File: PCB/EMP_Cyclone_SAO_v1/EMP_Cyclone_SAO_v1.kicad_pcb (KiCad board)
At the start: 2 copper layers, 72.8 x 84.4 mm, 7 parts, among them SW1 SW_Push, SW2 SW_Push, U3 ESP32-C3_SUPERMINI

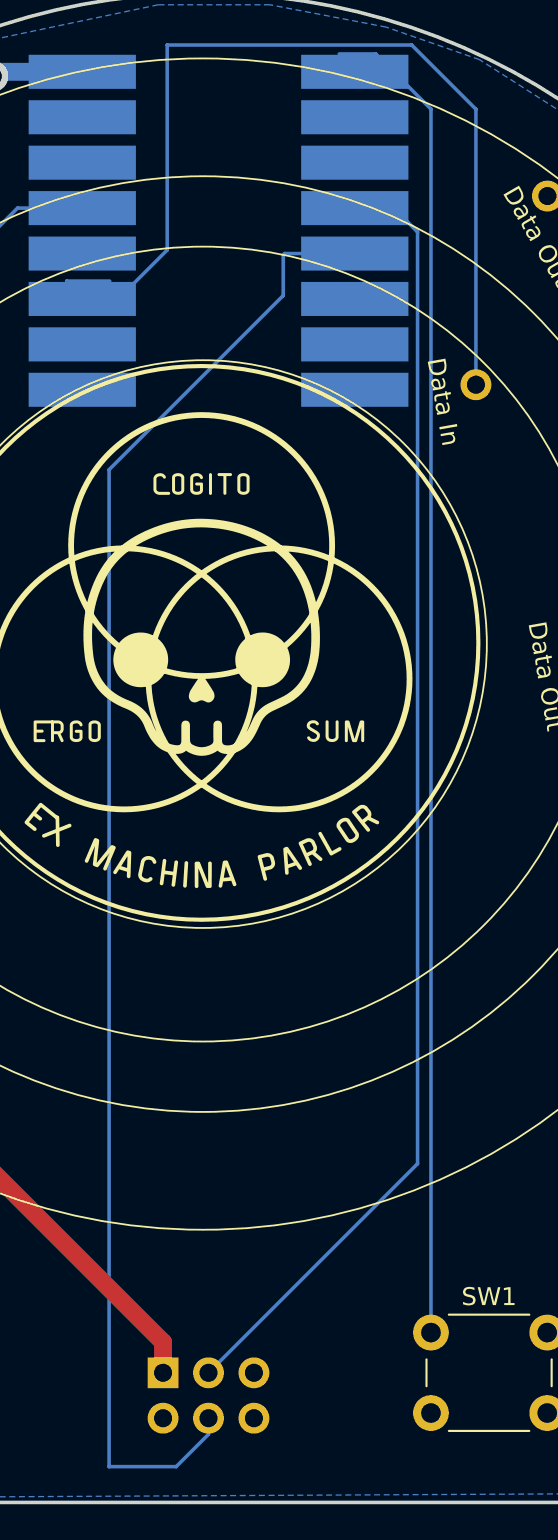
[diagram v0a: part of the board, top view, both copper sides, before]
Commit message: EMP SAO v2.1. Gerber files updated and ordered.
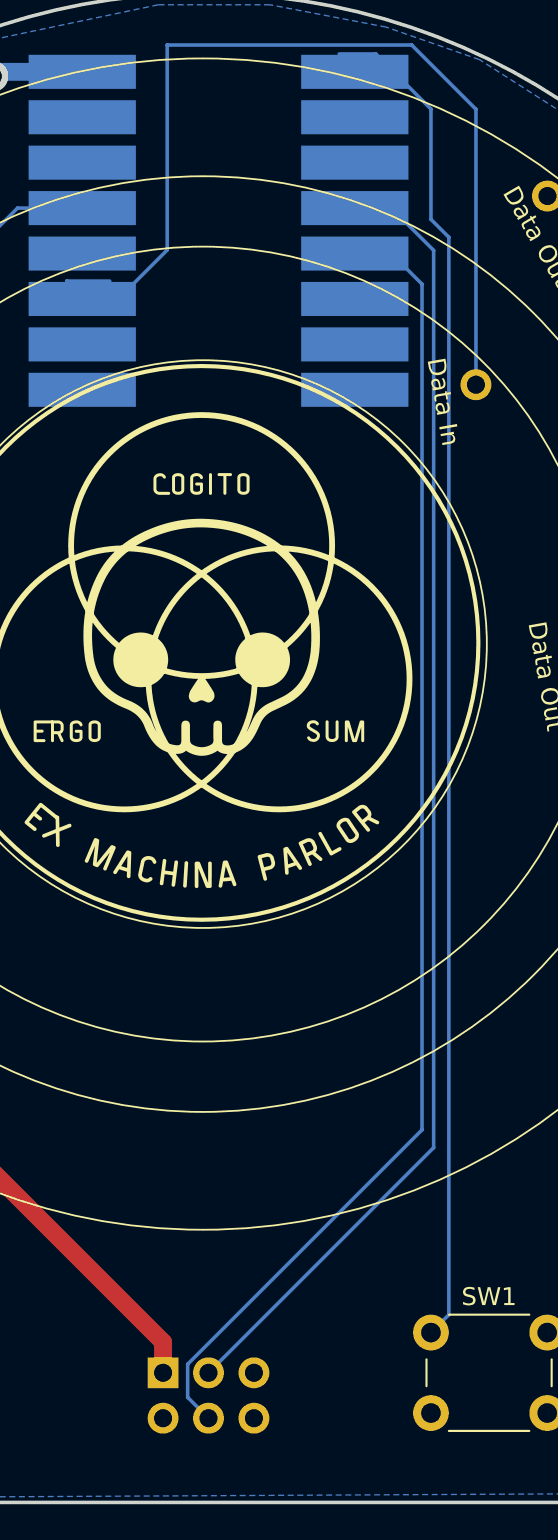
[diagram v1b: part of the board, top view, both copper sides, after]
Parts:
- moved G*** 0.25 mm to (100.0, 125.0), turned to 0 degrees
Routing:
- net unconnected-(U3-GPIO9-Pad9): track 83.0 -> 73.8 mm
- net Net-(U3-GPIO5): track 74.8 -> 75.7 mm
- net unconnected-(U3-GPIO8-Pad8): track 72.7 -> 73.4 mm
